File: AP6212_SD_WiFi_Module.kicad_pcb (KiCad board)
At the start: 2 copper layers, 24.6 x 23 mm, 22 parts, among them J1 Conn_Coaxial, J2 TF_Card, U1 AP6212, Y1 26MHz

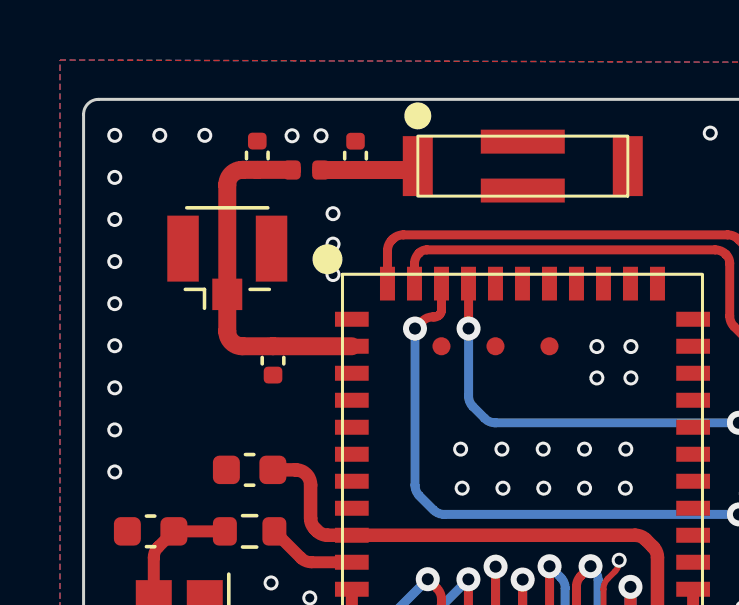
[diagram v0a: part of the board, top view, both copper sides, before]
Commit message: feat: The antenna line width is modified to 0.7 mm, and some gnd through holes are added
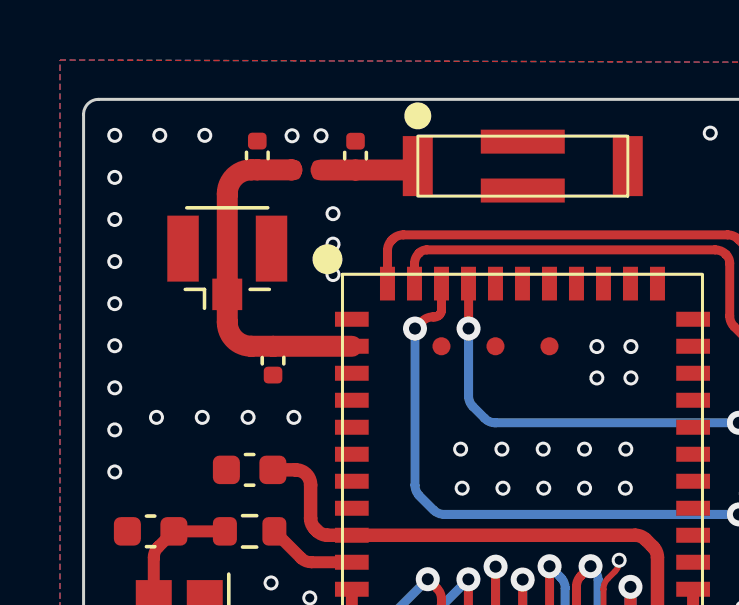
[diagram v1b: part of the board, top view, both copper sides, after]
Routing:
- net GND: vias 64 -> 68
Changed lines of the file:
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@@
   (segment (start 207.84 124.5175) (end 207.84 127.2) (width 0.45) (layer "F.Cu") (net 8))
   (segment (start 209.56 127.22) (end 207.86 127.22) (width 0.45) (layer "F.Cu") (net 8))
-  (segment (start 206.775 109.355) (end 208.72 109.355) (width 0.6) (layer "F.Cu") (net 9))
-  (segment (start 208.72 109.355) (end 208.85 109.225) (width 0.6) (layer "F.Cu") (net 9))
-  (segment (start 205.625 109.355) (end 206.775 109.355) (width 0.6) (layer "F.Cu") (net 9))
+  (segment (start 205.625 109.355) (end 206.775 109.355) (width 0.7) (layer "F.Cu") (net 9))
+  (segment (start 206.775 109.355) (end 208.72 109.355) (width 0.7) (layer "F.Cu") (net 9))
+  (segment (start 208.72 109.355) (end 208.85 109.225) (width 0.7) (layer "F.Cu") (net 9))
   (segment (start 215.04 124.5175) (end 215.04 123.328057) (width 0.2) (layer "F.Cu") (net 10))
   (segment (start 215.563 122.390843) (end 215.563 122.363) (width 0.2) (layer "F.Cu") (net 10))
@@
   (via (at 206.025 111.825) (size 0.5) (drill 0.3) (layers "F.Cu" "B.Cu") (free) (net 10))
   (via (at 209.345 134.15375) (size 0.5) (drill 0.3) (layers "F.Cu" "B.Cu") (free) (net 10))
+  (via (at 203.193332 117.6) (size 0.5) (drill 0.3) (layers "F.Cu" "B.Cu") (free) (net 10))
   (via (at 218.599667 108.125) (size 0.5) (drill 0.3) (layers "F.Cu" "B.Cu") (free) (net 10))
   (via (at 210.278 118.659) (size 0.5) (drill 0.3) (layers "F.Cu" "B.Cu") (free) (net 10))
@@
   (via (at 219.925 108.125) (size 0.5) (drill 0.3) (layers "F.Cu" "B.Cu") (free) (net 10))
   (via (at 211.689 119.96) (size 0.5) (drill 0.3) (layers "F.Cu" "B.Cu") (free) (net 10))
+  (via (at 204.72 117.6) (size 0.5) (drill 0.3) (layers "F.Cu" "B.Cu") (free) (net 10))
   (via (at 198.749 115.212125) (size 0.5) (drill 0.3) (layers "F.Cu" "B.Cu") (free) (net 10))
   (via (at 198.749 111.00425) (size 0.5) (drill 0.3) (layers "F.Cu" "B.Cu") (free) (net 10))
@@
   (via (at 215.955 115.24) (size 0.5) (drill 0.3) (layers "F.Cu" "B.Cu") (free) (net 10))
   (via (at 203.96 123.12) (size 0.5) (drill 0.3) (layers "F.Cu" "B.Cu") (free) (net 10))
+  (via (at 200.14 117.6) (size 0.5) (drill 0.3) (layers "F.Cu" "B.Cu") (free) (net 10))
   (via (at 205.25 123.62) (size 0.5) (drill 0.3) (layers "F.Cu" "B.Cu") (free) (net 10))
   (via (at 213.0315 118.659) (size 0.5) (drill 0.3) (layers "F.Cu" "B.Cu") (free) (net 10))
@@
   (via (at 221.25 110.675) (size 0.5) (drill 0.3) (layers "F.Cu" "B.Cu") (free) (net 10))
   (via (at 206.025 112.84) (size 0.5) (drill 0.3) (layers "F.Cu" "B.Cu") (free) (net 10))
+  (via (at 201.666666 117.6) (size 0.5) (drill 0.3) (layers "F.Cu" "B.Cu") (free) (net 10))
   (via (at 198.749 118.017375) (size 0.5) (drill 0.3) (layers "F.Cu" "B.Cu") (free) (net 10))
   (via (at 215.563 122.363) (size 0.5) (drill 0.3) (layers "F.Cu" "B.Cu") (free) (net 10))
@@
   (arc (start 215.416554 122.744396) (mid 215.52494 122.582184) (end 215.563 122.390843) (width 0.2) (layer "F.Cu") (net 10))
   (arc (start 215.186447 122.974503) (mid 215.07806 123.136715) (end 215.04 123.328057) (width 0.2) (layer "F.Cu") (net 10))
-  (segment (start 206.6525 115.23) (end 204.025 115.23) (width 0.6) (layer "F.Cu") (net 11))
-  (segment (start 204.65 109.35) (end 204.655 109.355) (width 0.6) (layer "F.Cu") (net 11))
-  (segment (start 202.5 114.73) (end 202.5 113.5) (width 0.6) (layer "F.Cu") (net 11))
-  (segment (start 203 109.35) (end 203.5 109.35) (width 0.6) (layer "F.Cu") (net 11))
-  (segment (start 202.5 113.5) (end 202.5 109.85) (width 0.6) (layer "F.Cu") (net 11))
-  (segment (start 204.025 115.23) (end 203 115.23) (width 0.6) (layer "F.Cu") (net 11))
-  (segment (start 203.5 109.35) (end 204.65 109.35) (width 0.6) (layer "F.Cu") (net 11))
-  (arc (start 203 115.23) (mid 202.646447 115.083553) (end 202.5 114.73) (width 0.6) (layer "F.Cu") (net 11))
-  (arc (start 202.5 109.85) (mid 202.646447 109.496447) (end 203 109.35) (width 0.6) (layer "F.Cu") (net 11))
+  (segment (start 206.6525 115.23) (end 204.025 115.23) (width 0.7) (layer "F.Cu") (net 11))
+  (segment (start 204.65 109.35) (end 204.655 109.355) (width 0.7) (layer "F.Cu") (net 11))
+  (segment (start 202.5 113.5) (end 202.5 110.15) (width 0.7) (layer "F.Cu") (net 11))
+  (segment (start 202.5 114.43) (end 202.5 113.5) (width 0.7) (layer "F.Cu") (net 11))
+  (segment (start 203.5 109.35) (end 204.65 109.35) (width 0.7) (layer "F.Cu") (net 11))
+  (segment (start 203.3 109.35) (end 203.5 109.35) (width 0.7) (layer "F.Cu") (net 11))
+  (segment (start 204.025 115.23) (end 203.3 115.23) (width 0.7) (layer "F.Cu") (net 11))
+  (arc (start 202.5 114.43) (mid 202.734315 114.995685) (end 203.3 115.23) (width 0.7) (layer "F.Cu") (net 11))
+  (arc (start 202.5 110.15) (mid 202.734315 109.584315) (end 203.3 109.35) (width 0.7) (layer "F.Cu") (net 11))
   (segment (start 215.94 124.5175) (end 215.94 123.25) (width 0.4) (layer "F.Cu") (net 12))
   (segment (start 216.34 127.22) (end 216.34 128.67) (width 0.4) (layer "F.Cu") (net 12))
